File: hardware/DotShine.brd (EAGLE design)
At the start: 30 x 65 mm, 56 parts, among them CN1 1X4-BIG, IC1 CAT24M010TS, IC3 SI1145, J3 USB-MICROB, U1 ATMEGA328P-MU-QFN32, U2 TMP102, U3 ATSHA204-TSU, X2 MC-RTC-RV-4162-C7-I2C, X3 S4B-ZR

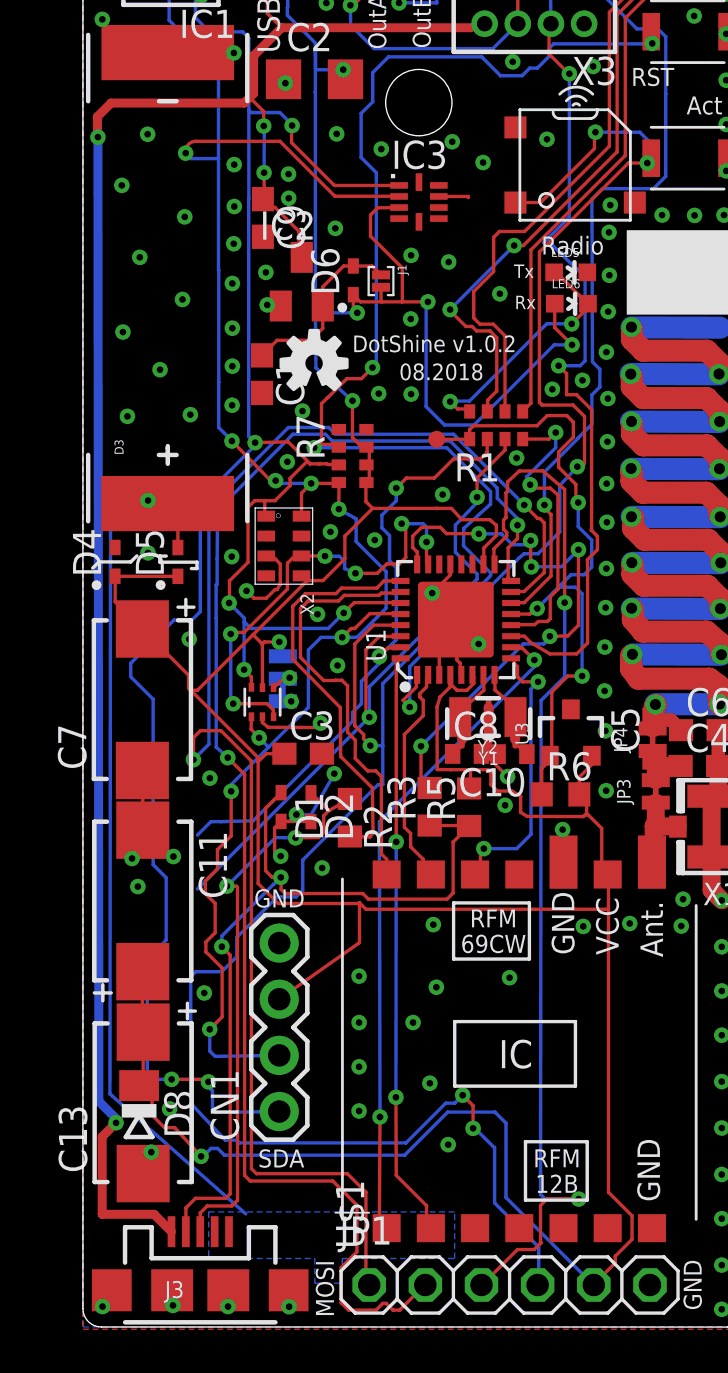
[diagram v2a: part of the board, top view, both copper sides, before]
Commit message: Rem superfluous Zener for solar, out it to LDO
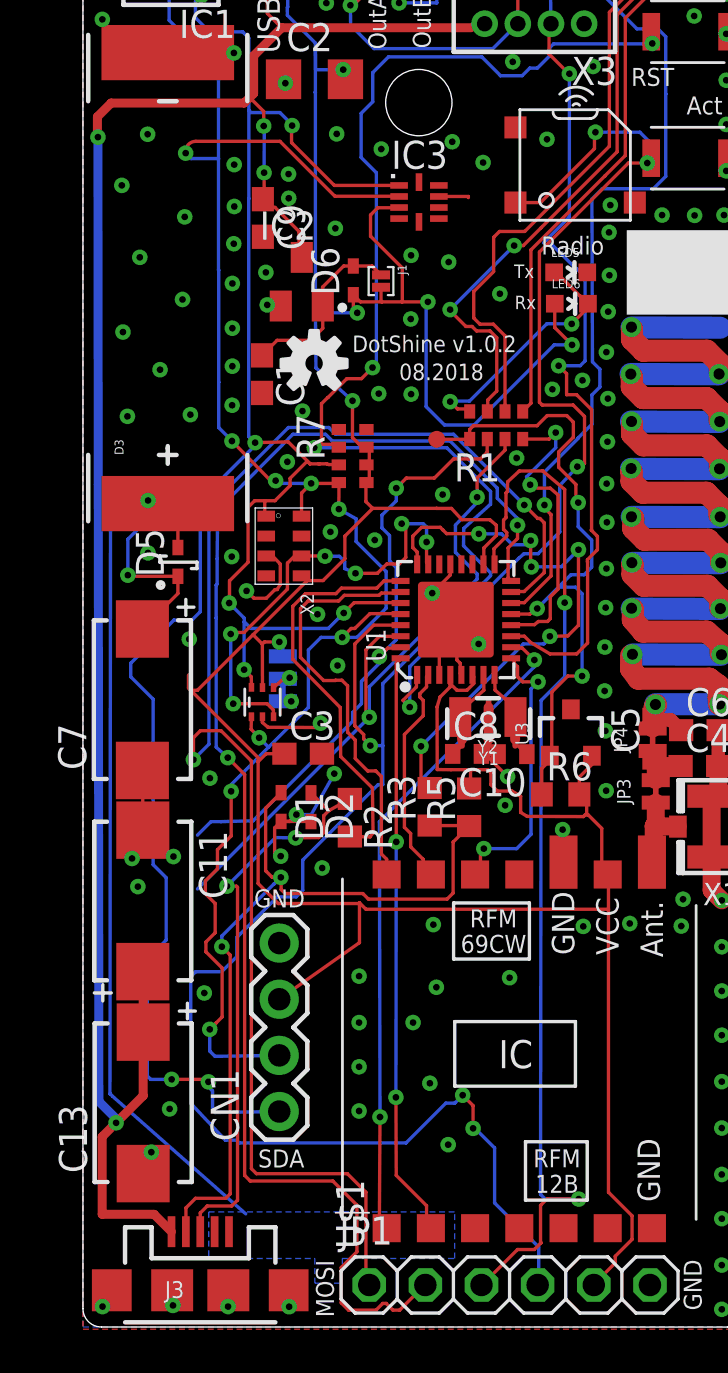
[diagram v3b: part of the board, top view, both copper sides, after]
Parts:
- removed D4: 3.6V Zener, diode:SOD523
- removed D8: 3.6V, diode:SOD80C
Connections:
- net +3V3: no longer C11.+, C13.+, C7.+, D4.C, D5.C, D8.C
- net +5V: now also C11.+, C13.+, C7.+, D5.C
- net GND: no longer D4.A, D8.A
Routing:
- net +3V3: track 237.0 -> 192.0 mm, vias 8 -> 7
- net +5V: track 87.1 -> 109.7 mm, vias 4 -> 5
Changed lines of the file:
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@@
 <layer number="46" name="Milling" color="3" fill="1" visible="no" active="yes"/>
 <layer number="47" name="Measures" color="7" fill="1" visible="no" active="yes"/>
-<layer number="48" name="Document" color="7" fill="1" visible="no" active="yes"/>
+<layer number="48" name="Document" color="7" fill="1" visible="yes" active="yes"/>
 <layer number="49" name="Reference" color="7" fill="1" visible="no" active="yes"/>
 <layer number="50" name="dxf" color="7" fill="1" visible="no" active="no"/>
@@
 <wire x1="5.159" y1="34.598" x2="5.159" y2="34.308" width="0.1524" layer="21"/>
 <wire x1="5.159" y1="34.308" x2="4.904" y2="34.308" width="0.1524" layer="21"/>
-<wire x1="0.439" y1="34.331" x2="0.724" y2="34.611" width="0.1524" layer="21"/>
-<wire x1="0.724" y1="34.611" x2="2.162" y2="34.611" width="0.1524" layer="21"/>
-<wire x1="2.162" y1="34.611" x2="2.443" y2="34.884" width="0.1524" layer="21"/>
 <text x="27.529" y="9.585" size="1.016" layer="22" rot="MR270">FSK</text>
 <text x="26.02" y="10.447" size="1.016" layer="22" rot="MR270">LoRA</text>
@@
 <wire x1="25.909" y1="5.625" x2="25.186" y2="5.625" width="0.1524" layer="22"/>
 <wire x1="25.186" y1="5.625" x2="25.186" y2="6.305" width="0.1524" layer="22"/>
-<circle x="0.615" y="33.558" radius="0.145028125" width="0.1524" layer="21"/>
-<circle x="0.638" y="33.534" radius="0.053" width="0.1524" layer="21"/>
 <circle x="3.516" y="33.564" radius="0.146453125" width="0.1524" layer="21"/>
 <circle x="3.557" y="33.546" radius="0.055971875" width="0.1524" layer="21"/>
@@
 <element name="U$3" library="pusbbutton_4x2_5" package="PUSHBUTTON_4X2.5" value="PUSHBUTTON_4X2.5" x="26.975" y="52.875"/>
 <element name="D3" library="SparkFun" package="SOLARBIT-12X1" value="Solar Cell 4V" x="3.837" y="47.45" rot="R90"/>
-<element name="D4" library="diode" package="SOD523" value="3.6V Zener" x="1.455" y="34.564" rot="R90"/>
 <element name="C11" library="adafruit" package="CT7343" value="1500uF 4V" x="2.707" y="19.276" rot="R270"/>
 <element name="C13" library="adafruit" package="CT7343" value="1500uF 4V" x="2.725" y="10.14" rot="R90"/>
@@
 <element name="D6" library="diode" package="SOD523" value="0.3V Schottky" x="12.232" y="47.296" rot="R90"/>
 <element name="J1" library="solderjumper" package="2.MED" value="" x="13.485" y="47.315" rot="R270"/>
-<element name="D8" library="diode" package="SOD80C" value="3.6V" x="2.54" y="9.2202" rot="R270"/>
 </elements>
 <signals>
@@
 <contactref element="C11" pad="-"/>
 <contactref element="C13" pad="-"/>
-<contactref element="D4" pad="A"/>
 <wire x1="1.13365625" y1="63.929865625" x2="1.6" y2="64.396209375" width="0.1524" layer="16"/>
 <contactref element="IC3" pad="8"/>
@@
 <via x="15.694" y="11.028" extent="1-16" drill="0.3"/>
 <via x="4.8092" y="31.1156" extent="1-16" drill="0.3"/>
-<contactref element="D8" pad="A"/>
-<wire x1="2.54" y1="7.5202" x2="2.159" y2="7.506" width="0.1524" layer="1"/>
 <wire x1="2.159" y1="7.506" x2="2.725" y2="6.94" width="0.1524" layer="1"/>
 </signal>
@@
 <wire x1="23.622" y1="20.574" x2="23.4696" y2="20.7264" width="0.1524" layer="1"/>
 <wire x1="23.622" y1="20.574" x2="23.74" y2="20.47" width="0.1524" layer="1"/>
-<wire x1="6.096" y1="8.0772" x2="6.4008" y2="7.7724" width="0.1524" layer="16"/>
-<wire x1="5.7912" y1="8.0772" x2="6.096" y2="8.0772" width="0.1524" layer="16"/>
-<wire x1="23.0124" y1="1.9812" x2="23.11" y2="1.9" width="0.1524" layer="16"/>
 <wire x1="23.7744" y1="6.096" x2="23.7744" y2="18.8976" width="0.1524" layer="1"/>
 <wire x1="23.7744" y1="18.8976" x2="23.7744" y2="20.4216" width="0.1524" layer="1"/>
@@
 <wire x1="14.29" y1="50.631" x2="13.337" y2="50.631" width="0.1524" layer="1"/>
 <wire x1="13.337" y1="50.631" x2="13.01" y2="50.304" width="0.1524" layer="1"/>
-<wire x1="3.692" y1="9.016" x2="4.147" y2="9.016" width="0.1524" layer="1"/>
-<wire x1="4.147" y1="9.016" x2="5.345" y2="7.718" width="0.1524" layer="1"/>
-<via x="5.345" y="7.718" extent="1-16" drill="0.3"/>
-<wire x1="5.345" y1="7.718" x2="5.545" y2="7.831" width="0.1524" layer="16"/>
-<wire x1="5.545" y1="7.831" x2="5.7912" y2="8.0772" width="0.1524" layer="16"/>
-<contactref element="C13" pad="+"/>
-<contactref element="C11" pad="+"/>
-<contactref element="D5" pad="C"/>
-<contactref element="D4" pad="C"/>
-<contactref element="C7" pad="+"/>
-<wire x1="4.296" y1="33.96" x2="1.459" y2="33.96" width="0.1524" layer="1"/>
-<wire x1="1.459" y1="33.96" x2="1.455" y2="33.964" width="0.1524" layer="1"/>
-<wire x1="2.633" y1="17.315" x2="2.707" y2="16.076" width="0.1524" layer="1"/>
-<wire x1="2.707" y1="16.076" x2="2.672" y2="13.622" width="0.1524" layer="1"/>
-<wire x1="2.672" y1="13.622" x2="2.725" y2="13.34" width="0.1524" layer="1"/>
 <wire x1="4.774" y1="28.9064" x2="4.774" y2="29.491" width="0.1524" layer="1"/>
-<wire x1="4.774" y1="29.491" x2="2.69" y2="31.575" width="0.1524" layer="1"/>
-<wire x1="1.459" y1="33.96" x2="1.459" y2="32.806" width="0.1524" layer="1"/>
-<wire x1="1.459" y1="32.806" x2="2.69" y2="31.575" width="0.1524" layer="1"/>
 <contactref element="J1" pad="2"/>
 <contactref element="D6" pad="C"/>
@@
 <wire x1="12.409" y1="45.879" x2="10.7566" y2="45.879" width="0.1524" layer="16"/>
 <wire x1="10.7566" y1="45.879" x2="10.5156" y2="46.12" width="0.1524" layer="16"/>
-<wire x1="2.216" y1="11.203" x2="2.972" y2="10.447" width="0.1524" layer="1" curve="90"/>
-<wire x1="2.972" y1="10.447" x2="3.125" y2="10.447" width="0.1524" layer="1"/>
-<wire x1="3.125" y1="10.447" x2="3.125" y2="9.583" width="0.1524" layer="1"/>
-<wire x1="3.125" y1="9.583" x2="3.692" y2="9.016" width="0.1524" layer="1"/>
-<wire x1="23.0124" y1="1.9812" x2="19.138" y2="5.8556" width="0.1524" layer="16"/>
-<wire x1="19.138" y1="5.8556" x2="19.138" y2="9.221" width="0.1524" layer="16"/>
-<wire x1="19.138" y1="9.221" x2="18.637" y2="9.722" width="0.1524" layer="16"/>
-<wire x1="18.637" y1="9.722" x2="16.504" y2="9.722" width="0.1524" layer="16"/>
-<wire x1="16.504" y1="9.722" x2="14.5544" y2="7.7724" width="0.1524" layer="16"/>
-<wire x1="14.5544" y1="7.7724" x2="6.4008" y2="7.7724" width="0.1524" layer="16"/>
 <wire x1="5.652840625" y1="61.727840625" x2="4.925" y2="61" width="0.1524" layer="16"/>
 <wire x1="4.925" y1="61" x2="3.5" y2="61" width="0.1524" layer="16"/>
@@
 <wire x1="5.1" y1="61.2" x2="6.0846875" y2="62.1846875" width="0.1524" layer="1"/>
 <wire x1="6.0846875" y1="62.1846875" x2="6.906446875" y2="62.1846875" width="0.1524" layer="1"/>
-<wire x1="4.296" y1="33.944" x2="4.296" y2="33.96" width="0.1524" layer="1"/>
-<contactref element="D8" pad="C"/>
-<wire x1="2.54" y1="10.9202" x2="2.159" y2="11.146" width="0.1524" layer="1"/>
-<wire x1="2.159" y1="11.146" x2="2.216" y2="11.203" width="0.1524" layer="1"/>
-<wire x1="2.216" y1="11.203" x2="2.725" y2="11.203" width="0.1524" layer="1"/>
-<wire x1="2.725" y1="11.203" x2="2.725" y2="13.34" width="0.1524" layer="1"/>
 </signal>
 <signal name="ADCENA">
@@
 <wire x1="0.655" y1="53.85" x2="0.678" y2="53.827" width="0.4064" layer="1"/>
 <via x="0.678" y="53.827" extent="1-16" drill="0.3"/>
-<wire x1="0.678" y1="53.827" x2="0.721" y2="10.205" width="0.4064" layer="16"/>
+<wire x1="0.678" y1="53.827" x2="0.693503125" y2="38.09950625" width="0.4064" layer="16"/>
+<wire x1="0.693503125" y1="38.09950625" x2="0.721" y2="10.205" width="0.4064" layer="16"/>
 <wire x1="0.87" y1="5.098" x2="3.219725" y2="5.098" width="0.4064" layer="1"/>
 <wire x1="3.219725" y1="5.098" x2="4.006565625" y2="4.311159375" width="0.4064" layer="1"/>
@@
 <wire x1="8.343165625" y1="60.967659375" x2="8.343165625" y2="59.422034375" width="0.1524" layer="1"/>
 <wire x1="8.343165625" y1="59.422034375" x2="8.9906" y2="58.7746" width="0.1524" layer="1"/>
+<contactref element="D5" pad="C"/>
+<contactref element="C11" pad="+"/>
+<contactref element="C13" pad="+"/>
+<contactref element="C7" pad="+"/>
+<wire x1="2.725" y1="13.34" x2="2.725" y2="10.461" width="0.4064" layer="1"/>
+<wire x1="2.725" y1="10.461" x2="1.5" y2="9.236" width="0.4064" layer="1"/>
+<wire x1="2.725" y1="13.34" x2="2.725" y2="16.058" width="0.4064" layer="1"/>
+<wire x1="2.725" y1="16.058" x2="2.707" y2="16.076" width="0.4064" layer="1"/>
+<wire x1="4.296" y1="33.96" x2="4.296" y2="33.181" width="0.1524" layer="1"/>
+<wire x1="4.296" y1="33.181" x2="2.69" y2="31.575" width="0.1524" layer="1"/>
+<wire x1="4.296" y1="33.96" x2="2.2604" y2="33.96" width="0.1524" layer="1"/>
+<wire x1="2.2604" y1="33.96" x2="2.2352" y2="33.9852" width="0.1524" layer="1"/>
+<wire x1="2.2352" y1="33.9852" x2="2.0574" y2="33.9852" width="0.1524" layer="1"/>
+<wire x1="2.0574" y1="33.9852" x2="2.032" y2="34.0106" width="0.1524" layer="1"/>
+<via x="2.032" y="34.0106" extent="1-16" drill="0.3"/>
+<wire x1="2.032" y1="34.0106" x2="2.032" y2="35.6362" width="0.1524" layer="16"/>
+<wire x1="2.032" y1="35.6362" x2="2.5654" y2="36.1696" width="0.1524" layer="16"/>
+<wire x1="2.5654" y1="36.1696" x2="3.8608" y2="36.1696" width="0.1524" layer="16"/>
+<wire x1="3.8608" y1="36.1696" x2="4.8768" y2="37.1856" width="0.1524" layer="16"/>
+<wire x1="4.8768" y1="37.1856" x2="4.8768" y2="37.4396" width="0.1524" layer="16"/>
+<wire x1="4.8768" y1="37.4396" x2="4.2926" y2="38.0238" width="0.1524" layer="16"/>
+<wire x1="4.2926" y1="38.0238" x2="0.769209375" y2="38.0238" width="0.1524" layer="16"/>
+<wire x1="0.769209375" y1="38.0238" x2="0.693503125" y2="38.09950625" width="0.1524" layer="16"/>
 </signal>
 <signal name="N$7">
@@
 <signal name="N$5">
 </signal>
-<signal name="N$33">
-</signal>
 </signals>

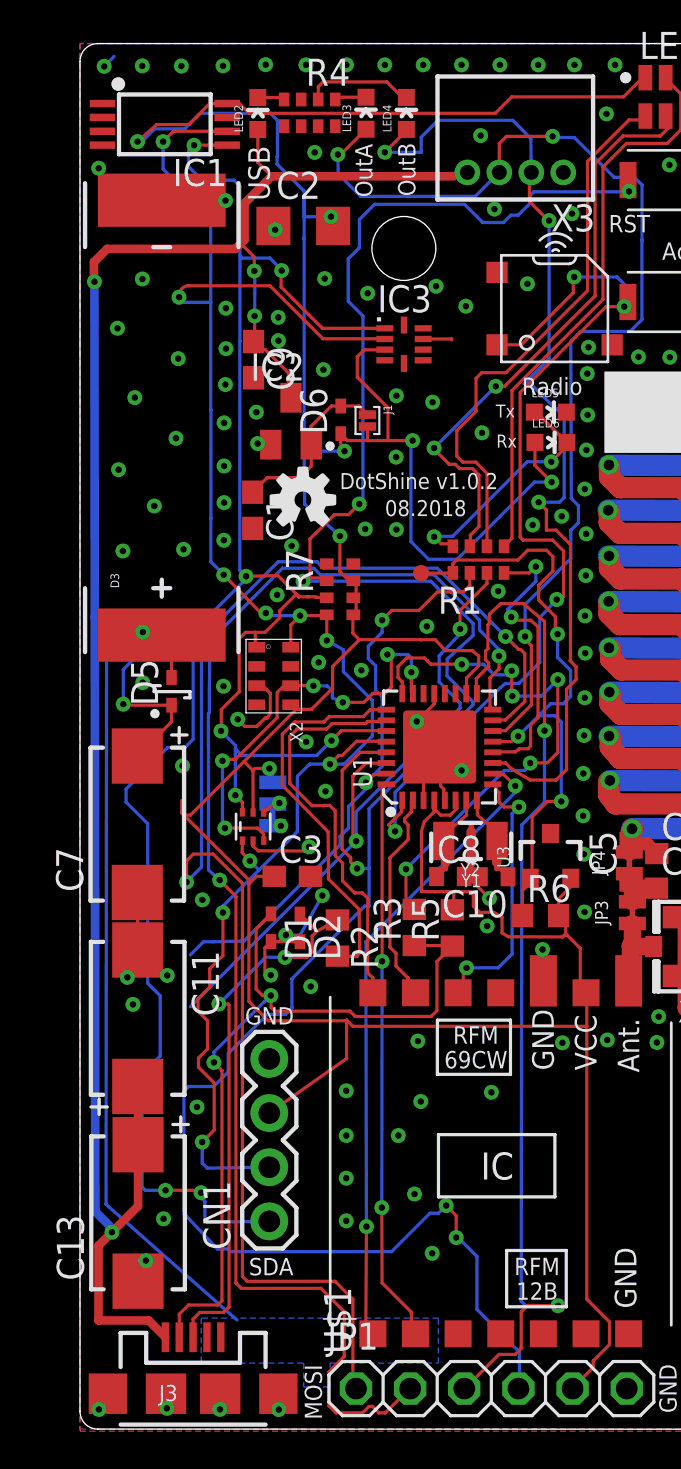
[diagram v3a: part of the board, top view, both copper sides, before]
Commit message: Separate USB Led from solar
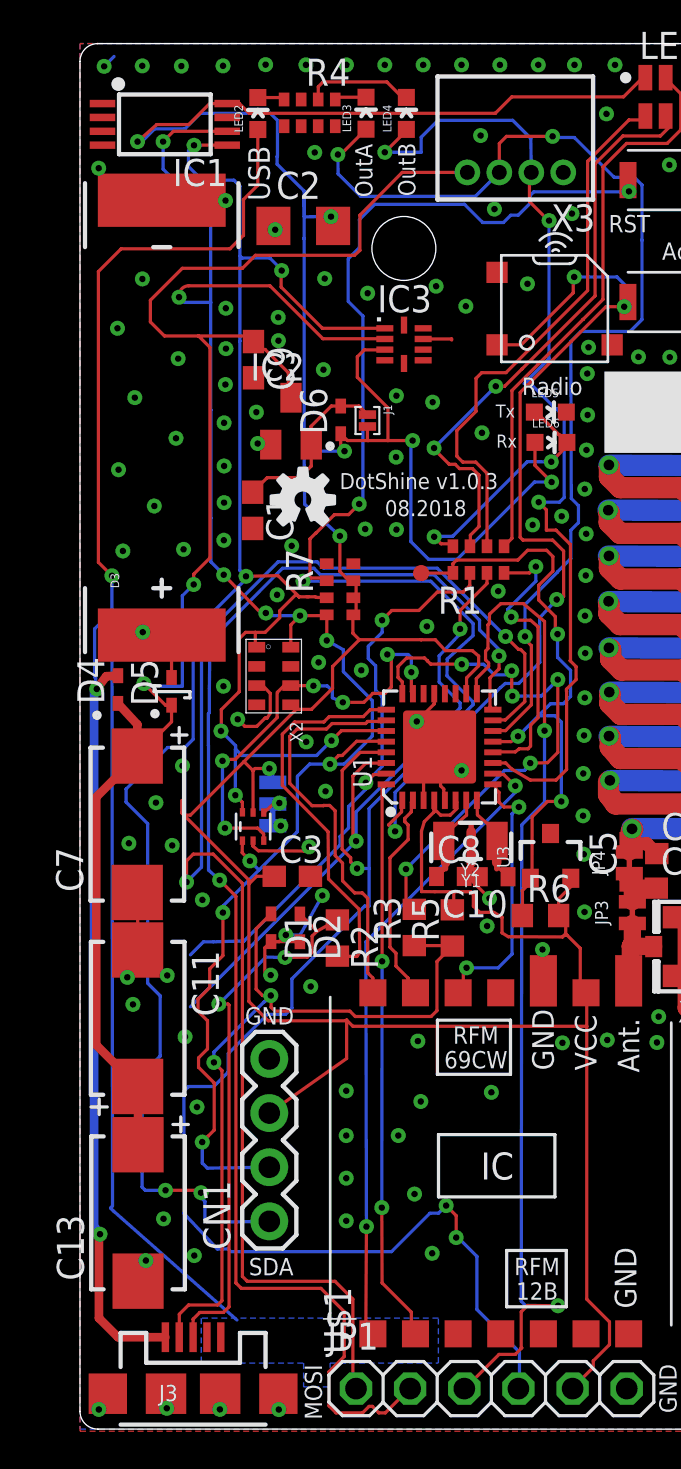
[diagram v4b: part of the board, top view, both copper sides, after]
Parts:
- added D4: 0.3V Schottky, diode:SOD523
- R1: value (none) -> 470Ω
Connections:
- new net USB_FOR_LED: D4.A, J3.VBUS, LED2.A
- net +5V: now also D4.C; no longer J3.VBUS, LED2.A
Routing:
- net USB_FOR_LED: track 0.00 -> 67.5 mm, vias 0 -> 3
- net +5V: track 109.7 -> 74.5 mm, vias 5 -> 2
- net GND: vias 140 -> 144
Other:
- board text added: "DotShine v1.0.3"
- board text removed: "DotShine v1.0.2"
